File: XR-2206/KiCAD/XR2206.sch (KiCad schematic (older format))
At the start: 15 parts, among them J1 CONN_3, J2 CONN_2, U1 XR2206

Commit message: updating theremin related files
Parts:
- removed C3: 1UF, symbol CAPAPOL
- added C3: 1uF, symbol CP1
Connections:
- wire segments 41 -> 52
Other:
- note added: "S\nV\nG"
- note removed: "G\nV\nS"
- moved on the sheet: C1, C2, J1, J2, MTG1, MTG2, R1, R2, R3, R4, R5, R6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

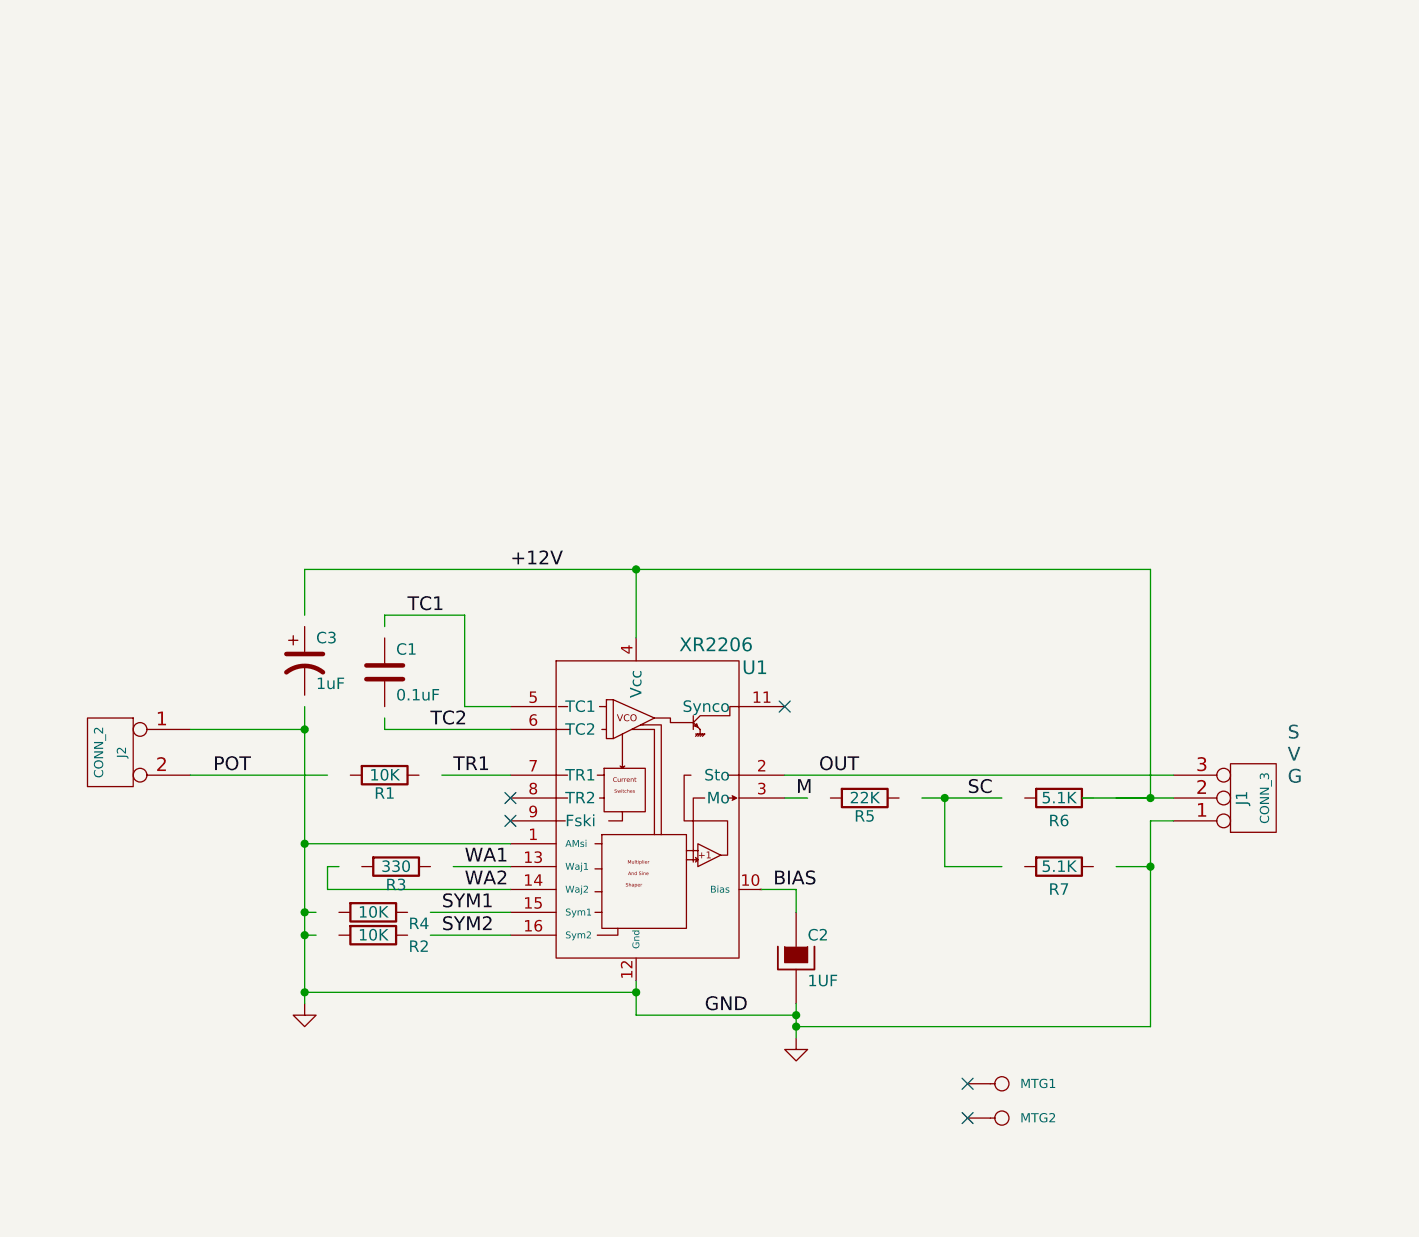
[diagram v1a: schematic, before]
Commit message: Worked on X3 version of XR-2206 and X3 version of BrBdPwrSply
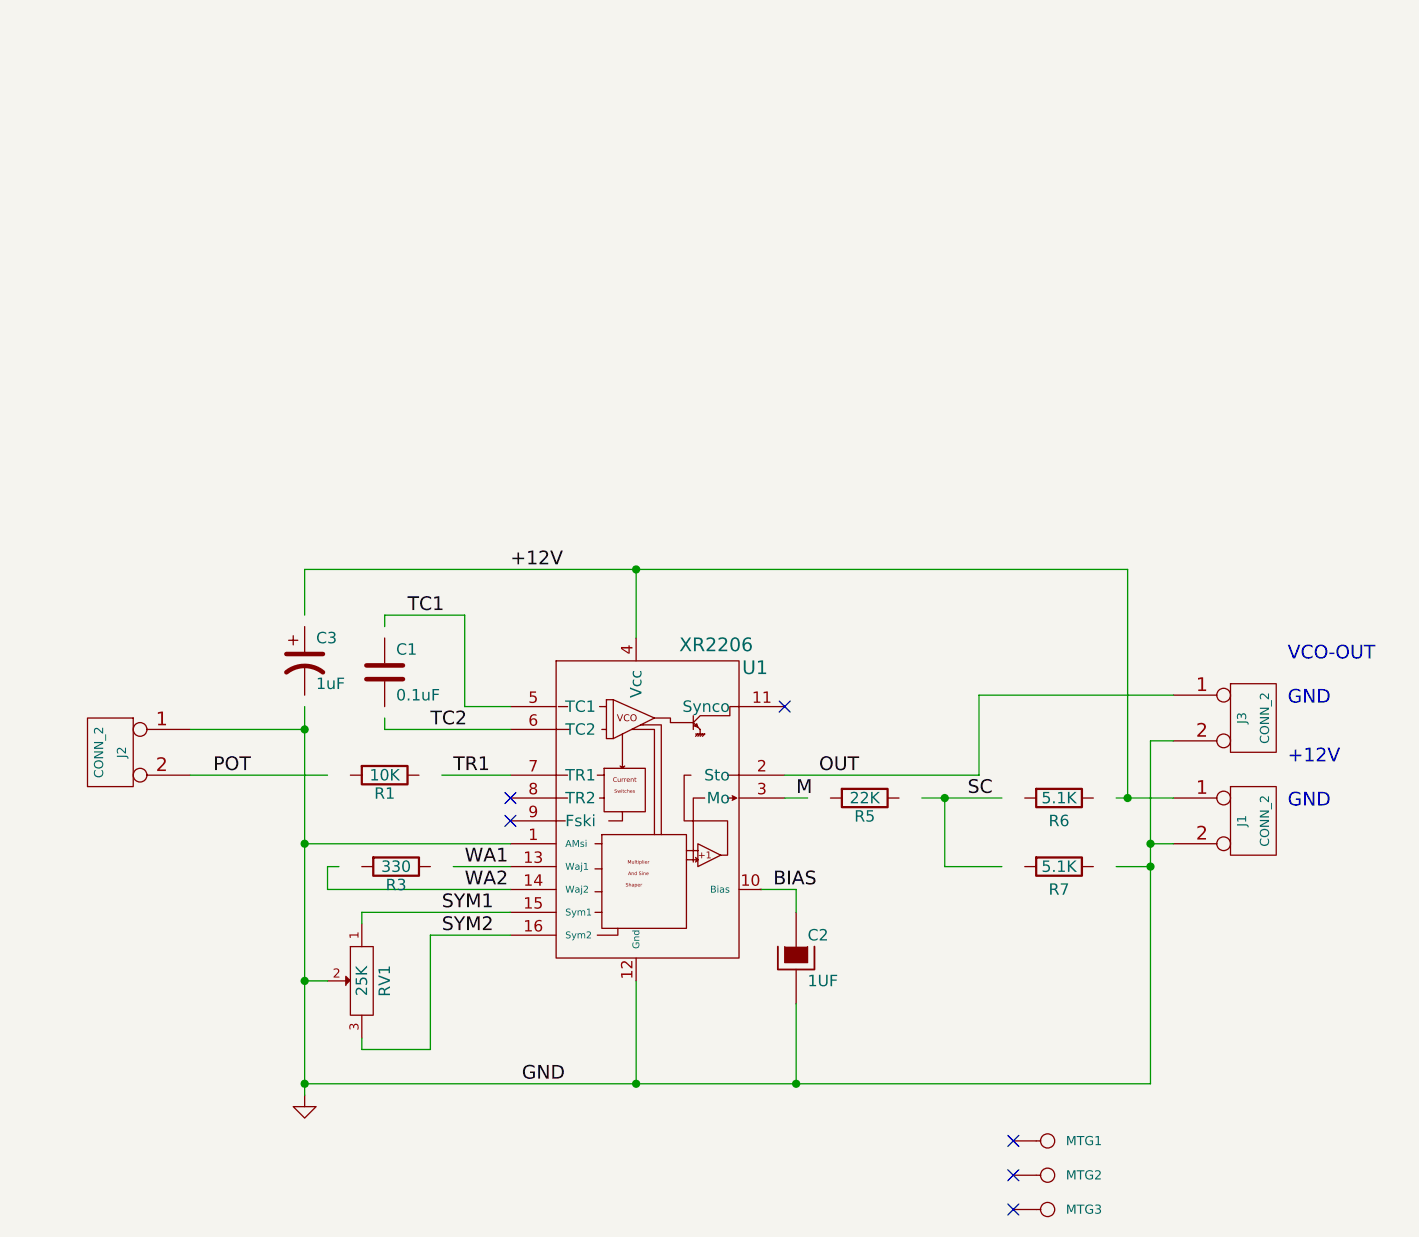
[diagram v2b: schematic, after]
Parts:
- removed J1: CONN_3, symbol CONN_3
- removed R2, R4: 10K, symbol R
- added J1, J3: CONN_2, symbol CONN_2
- added MTG3: CONN_1, symbol CONN_1
- added RV1: 25K, symbol POT
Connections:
- wire segments 52 -> 43
- no-connect marks 5 -> 6
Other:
- note added: "+12V\n\nGND"
- note added: "VCO-OUT\n\nGND"
- note removed: "S\nV\nG"
- moved on the sheet: MTG1, MTG2
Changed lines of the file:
@@
-EESchema Schematic File Version 2  date 13/02/2013 09:23:48
+EESchema Schematic File Version 2  date 15/02/2013 13:58:34
 LIBS:power
 LIBS:device
@@
 Sheet 1 1
 Title "XR-2206"
-Date "13 feb 2013"
+Date "15 feb 2013"
 Rev "X2"
 Comp ""
@@
 Comment4 ""
 $EndDescr
+NoConn ~ 6950 5750
+$Comp
+L CONN_1 MTG3
+U 1 1 511E84D9
+P 7100 5750
+F 0 "MTG3" H 7180 5750 40  0000 L CNN
+F 1 "CONN_1" H 7100 5805 30  0001 C CNN
+	1    7100 5750
+	1    0    0    -1
+$EndComp
+Wire Wire Line
+	7400 3950 7650 3950
+Wire Wire Line
+	7650 3500 6800 3500
+Wire Wire Line
+	6800 3500 6800 3850
+Wire Wire Line
+	6800 3850 5950 3850
+Wire Wire Line
+	4400 5050 4400 4550
+Wire Wire Line
+	4400 5050 4100 5050
+Wire Wire Line
+	4100 5050 4100 5000
+Wire Wire Line
+	4100 4500 4100 4450
+Wire Wire Line
+	4100 4450 4750 4450
+Connection ~ 6650 3950
+Wire Wire Line
+	6550 3950 6900 3950
+Connection ~ 3850 3650
+Wire Wire Line
+	3350 3650 3850 3650
+Connection ~ 5300 5200
+Wire Wire Line
+	5300 4750 5300 5200
+Wire Wire Line
+	7450 2950 3850 2950
+Wire Wire Line
+	7450 2950 7450 3950
+Wire Wire Line
+	4400 4550 4750 4550
+Wire Wire Line
+	4750 4250 4500 4250
+Connection ~ 3850 5200
+Wire Wire Line
+	5300 3250 5300 2950
+Wire Wire Line
+	3850 2950 3850 3150
+Wire Wire Line
+	6000 5200 6000 4850
+Wire Wire Line
+	4200 3200 4200 3150
+Wire Wire Line
+	4200 3150 4550 3150
+Wire Wire Line
+	4550 3150 4550 3550
+Wire Wire Line
+	4550 3550 4750 3550
+Wire Wire Line
+	4450 3850 4750 3850
+Wire Wire Line
+	4750 3650 4200 3650
+Wire Wire Line
+	4200 3650 4200 3600
+Wire Wire Line
+	5850 4350 6000 4350
+Wire Wire Line
+	6000 4350 6000 4450
+Wire Wire Line
+	3850 4150 4750 4150
+Connection ~ 3850 4150
+Connection ~ 5300 2950
+Wire Wire Line
+	3850 5250 3850 3550
+Wire Wire Line
+	4750 4350 3950 4350
+Wire Wire Line
+	3950 4350 3950 4250
+Wire Wire Line
+	3950 4250 4000 4250
+Wire Wire Line
+	3850 5200 7550 5200
+Connection ~ 6000 5200
+Wire Wire Line
+	7550 4150 7650 4150
+Wire Wire Line
+	3950 3850 3350 3850
+Connection ~ 7450 3950
+Wire Wire Line
+	6900 4250 6650 4250
+Wire Wire Line
+	6650 4250 6650 3950
+Wire Wire Line
+	5950 3950 6050 3950
+Wire Wire Line
+	7400 4250 7550 4250
 Connection ~ 7550 4250
 Wire Wire Line
-	7400 4250 7550 4250
-Wire Wire Line
-	5950 3950 6050 3950
-Wire Wire Line
-	6650 3950 6650 4250
-Wire Wire Line
-	6650 4250 6900 4250
-Connection ~ 7550 3950
-Wire Wire Line
-	7400 3950 7550 3950
-Wire Wire Line
-	3950 3850 3350 3850
-Wire Wire Line
-	7650 4050 7550 4050
-Connection ~ 6000 4950
-Wire Wire Line
-	6000 4950 7550 4950
-Wire Wire Line
-	5950 3850 7650 3850
-Connection ~ 3850 4450
-Wire Wire Line
-	3850 4450 3900 4450
-Wire Wire Line
-	4000 4250 3950 4250
-Wire Wire Line
-	3950 4250 3950 4350
-Wire Wire Line
-	3950 4350 4750 4350
-Wire Wire Line
-	3850 4850 3850 4800
-Wire Wire Line
-	3850 4800 3850 4550
-Wire Wire Line
-	3850 4550 3850 4450
-Wire Wire Line
-	3850 4450 3850 4150
-Wire Wire Line
-	3850 4150 3850 3650
-Wire Wire Line
-	3850 3650 3850 3550
-Connection ~ 5300 2950
-Connection ~ 3850 4150
-Wire Wire Line
-	3850 4150 4750 4150
-Wire Wire Line
-	6000 4450 6000 4350
-Wire Wire Line
-	6000 4350 5850 4350
-Wire Wire Line
-	4200 3600 4200 3650
-Wire Wire Line
-	4200 3650 4750 3650
-Wire Wire Line
-	4450 3850 4750 3850
-Wire Wire Line
-	4750 3550 4550 3550
-Wire Wire Line
-	4550 3550 4550 3150
-Wire Wire Line
-	4550 3150 4200 3150
-Wire Wire Line
-	4200 3150 4200 3200
-Wire Wire Line
-	6000 4850 6000 4900
-Wire Wire Line
-	6000 4900 6000 4950
-Wire Wire Line
-	6000 4950 6000 5000
-Wire Wire Line
-	3850 3150 3850 2950
-Wire Wire Line
-	5300 3250 5300 2950
-Wire Wire Line
-	5300 4800 3850 4800
-Connection ~ 3850 4800
-Wire Wire Line
-	4750 4250 4500 4250
-Wire Wire Line
-	4750 4450 4400 4450
-Wire Wire Line
-	3850 4550 3900 4550
-Connection ~ 3850 4550
-Wire Wire Line
-	4400 4550 4750 4550
-Wire Wire Line
-	7550 3950 7550 2950
-Wire Wire Line
-	7250 3950 7550 3950
-Wire Wire Line
-	7550 3950 7650 3950
-Wire Wire Line
-	7550 2950 5300 2950
-Wire Wire Line
-	5300 2950 3850 2950
-Wire Wire Line
-	6000 4900 5300 4900
-Wire Wire Line
-	5300 4900 5300 4800
-Wire Wire Line
-	5300 4800 5300 4750
-Connection ~ 5300 4800
-Connection ~ 6000 4900
-Wire Wire Line
-	3850 3650 3350 3650
-Connection ~ 3850 3650
-Wire Wire Line
-	6550 3950 6650 3950
-Wire Wire Line
-	6650 3950 6900 3950
-Connection ~ 6650 3950
-Wire Wire Line
-	7550 4950 7550 4250
-Wire Wire Line
-	7550 4250 7550 4050
+	3850 4750 3950 4750
+Connection ~ 3850 4750
+Wire Wire Line
+	7550 5200 7550 3700
+Wire Wire Line
+	7550 3700 7650 3700
+Connection ~ 7550 4150
+Text Notes 8150 3550 0    60   ~ 0
+VCO-OUT\n\nGND
+$Comp
+L CONN_2 J3
+U 1 1 511E7A29
+P 8000 3600
+F 0 "J3" V 7950 3600 40  0000 C CNN
+F 1 "CONN_2" V 8050 3600 40  0000 C CNN
+	1    8000 3600
+	1    0    0    -1
+$EndComp
+$Comp
+L CONN_2 J1
+U 1 1 511E7A25
+P 8000 4050
+F 0 "J1" V 7950 4050 40  0000 C CNN
+F 1 "CONN_2" V 8050 4050 40  0000 C CNN
+	1    8000 4050
+	1    0    0    -1
+$EndComp
+$Comp
+L POT RV1
+U 1 1 511E791A
+P 4100 4750
+F 0 "RV1" H 4100 4650 50  0000 C CNN
+F 1 "25K" H 4100 4750 50  0000 C CNN
+	1    4100 4750
+	0    -1   1    0
+$EndComp
 $Comp
 L CP1 C3
@@
 L CONN_1 MTG2
 U 1 1 501125B1
-P 6900 5350
-F 0 "MTG2" H 6980 5350 40  0000 L CNN
-F 1 "CONN_1" H 6900 5405 30  0001 C CNN
-	1    6900 5350
-	1    0    0    -1
-$EndComp
-NoConn ~ 6750 5350
+P 7100 5600
+F 0 "MTG2" H 7180 5600 40  0000 L CNN
+F 1 "CONN_1" H 7100 5655 30  0001 C CNN
+	1    7100 5600
+	1    0    0    -1
+$EndComp
+NoConn ~ 6950 5600
 $Comp
 L R R5
@@
 	-1   0    0    -1
 $EndComp
-Text Notes 8150 3900 0    60   ~ 0
-S\nV\nG
-NoConn ~ 6750 5200
+Text Notes 8150 4000 0    60   ~ 0
++12V\n\nGND
+NoConn ~ 6950 5450
 $Comp
 L CONN_1 MTG1
 U 1 1 4FDBED61
-P 6900 5200
-F 0 "MTG1" H 6980 5200 40  0000 L CNN
-F 1 "CONN_1" H 6900 5255 30  0001 C CNN
-	1    6900 5200
-	1    0    0    -1
-$EndComp
-Text Label 5600 4900 0    60   ~ 0
+P 7100 5450
+F 0 "MTG1" H 7180 5450 40  0000 L CNN
+F 1 "CONN_1" H 7100 5505 30  0001 C CNN
+	1    7100 5450
+	1    0    0    -1
+$EndComp
+Text Label 4800 5200 0    60   ~ 0
 GND
 Text Label 4750 2950 0    60   ~ 0
@@
 NoConn ~ 4750 4050
 NoConn ~ 4750 3950
-$Comp
-L CONN_3 J1
-U 1 1 4FDBE66A
-P 8000 3950
-F 0 "J1" V 7950 3950 50  0000 C CNN
-F 1 "CONN_3" V 8050 3950 40  0000 C CNN
-	1    8000 3950
-	1    0    0    1
-$EndComp
-$Comp
-L R R2
-U 1 1 4FDBE59E
-P 4150 4550
-F 0 "R2" V 4200 4750 50  0000 C CNN
-F 1 "10K" V 4150 4550 50  0000 C CNN
-	1    4150 4550
-	0    1    1    0
-$EndComp
-$Comp
-L R R4
-U 1 1 4FDBE58B
-P 4150 4450
-F 0 "R4" V 4200 4650 50  0000 C CNN
-F 1 "10K" V 4150 4450 50  0000 C CNN
-	1    4150 4450
-	0    1    1    0
-$EndComp
 $Comp
 L R R3
@@
 $EndComp
 $Comp
-L GND #PWR01
-U 1 1 4FDBC7B9
-P 6000 5000
-F 0 "#PWR01" H 6000 5000 30  0001 C CNN
-F 1 "GND" H 6000 4930 30  0001 C CNN
-	1    6000 5000
-	1    0    0    -1
-$EndComp
-$Comp
 L CAPAPOL C2
 U 1 1 4FDBC7A6
@@
 $EndComp
 $Comp
-L GND #PWR02
+L GND #PWR01
 U 1 1 4FDBC71A
-P 3850 4850
-F 0 "#PWR02" H 3850 4850 30  0001 C CNN
-F 1 "GND" H 3850 4780 30  0001 C CNN
-	1    3850 4850
-	1    0    0    -1
-$EndComp
+P 3850 5250
+F 0 "#PWR01" H 3850 5250 30  0001 C CNN
+F 1 "GND" H 3850 5180 30  0001 C CNN
+	1    3850 5250
+	1    0    0    -1
+$EndComp

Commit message: Integr theremin
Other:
- note added: "G\n\nADJ"
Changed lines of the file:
@@
-EESchema Schematic File Version 2  date 15/02/2013 13:58:34
+EESchema Schematic File Version 2  date Fri 15 Feb 2013 06:24:37 PM EST
 LIBS:power
 LIBS:device
@@
 LIBS:atmel
 LIBS:contrib
-LIBS:EXAR
 LIBS:XR2206-cache
 EELAYER 25  0
@@
 Comment4 ""
 $EndDescr
+Text Notes 2850 3700 2    60   ~ 0
+G\n\nADJ
 NoConn ~ 6950 5750
 $Comp

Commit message: Updated libraries and XR-2206 board schematic
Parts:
- C3: value 1uF -> 4.7uF
- R3: value 330 -> 220
- R5: value 22K -> 10K
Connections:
- wire segments 43 -> 42
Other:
- moved on the sheet: J1, J3
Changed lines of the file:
@@
-EESchema Schematic File Version 2  date Fri 15 Feb 2013 06:24:37 PM EST
+EESchema Schematic File Version 2  date 06/03/2013 12:50:37
 LIBS:power
 LIBS:device
@@
 LIBS:contrib
 LIBS:XR2206-cache
-EELAYER 25  0
+EELAYER 27 0
 EELAYER END
 $Descr A 11000 8500
@@
 Sheet 1 1
 Title "XR-2206"
-Date "15 feb 2013"
-Rev "X2"
+Date "6 mar 2013"
+Rev "X3"
 Comp ""
 Comment1 ""
@@
 F 0 "MTG3" H 7180 5750 40  0000 L CNN
 F 1 "CONN_1" H 7100 5805 30  0001 C CNN
+F 2 "" H 7100 5750 60  0001 C CNN
+F 3 "" H 7100 5750 60  0001 C CNN
 	1    7100 5750
 	1    0    0    -1
 $EndComp
 Wire Wire Line
-	7400 3950 7650 3950
-Wire Wire Line
-	7650 3500 6800 3500
-Wire Wire Line
-	6800 3500 6800 3850
+	3850 2950 7700 2950
+Wire Wire Line
+	7650 3850 6800 3850
 Wire Wire Line
 	6800 3850 5950 3850
@@
 Wire Wire Line
 	5300 4750 5300 5200
-Wire Wire Line
-	7450 2950 3850 2950
 Wire Wire Line
 	7450 2950 7450 3950
@@
 	3950 4250 4000 4250
 Wire Wire Line
-	3850 5200 7550 5200
+	7550 5200 3850 5200
 Connection ~ 6000 5200
 Wire Wire Line
-	7550 4150 7650 4150
+	7550 3150 7700 3150
 Wire Wire Line
 	3950 3850 3350 3850
-Connection ~ 7450 3950
 Wire Wire Line
 	6900 4250 6650 4250
@@
 Connection ~ 3850 4750
 Wire Wire Line
-	7550 5200 7550 3700
-Wire Wire Line
-	7550 3700 7650 3700
-Connection ~ 7550 4150
-Text Notes 8150 3550 0    60   ~ 0
+	7550 3150 7550 5200
+Wire Wire Line
+	7550 4050 7650 4050
+Text Notes 8150 3900 0    60   ~ 0
 VCO-OUT\n\nGND
 $Comp
 L CONN_2 J3
 U 1 1 511E7A29
-P 8000 3600
-F 0 "J3" V 7950 3600 40  0000 C CNN
-F 1 "CONN_2" V 8050 3600 40  0000 C CNN
-	1    8000 3600
+P 8000 3950
+F 0 "J3" V 7950 3950 40  0000 C CNN
+F 1 "CONN_2" V 8050 3950 40  0000 C CNN
+F 2 "" H 8000 3950 60  0001 C CNN
+F 3 "" H 8000 3950 60  0001 C CNN
+	1    8000 3950
 	1    0    0    -1
 $EndComp
@@
 L CONN_2 J1
 U 1 1 511E7A25
-P 8000 4050
-F 0 "J1" V 7950 4050 40  0000 C CNN
-F 1 "CONN_2" V 8050 4050 40  0000 C CNN
-	1    8000 4050
+P 8050 3050
+F 0 "J1" V 8000 3050 40  0000 C CNN
+F 1 "CONN_2" V 8100 3050 40  0000 C CNN
+F 2 "" H 8050 3050 60  0001 C CNN
+F 3 "" H 8050 3050 60  0001 C CNN
+	1    8050 3050
 	1    0    0    -1
 $EndComp
@@
 F 0 "RV1" H 4100 4650 50  0000 C CNN
 F 1 "25K" H 4100 4750 50  0000 C CNN
+F 2 "" H 4100 4750 60  0001 C CNN
+F 3 "" H 4100 4750 60  0001 C CNN
 	1    4100 4750
 	0    -1   1    0
@@
 P 3850 3350
 F 0 "C3" H 3900 3450 50  0000 L CNN
-F 1 "1uF" H 3900 3250 50  0000 L CNN
+F 1 "4.7uF" H 3900 3250 50  0000 L CNN
+F 2 "" H 3850 3350 60  0001 C CNN
+F 3 "" H 3850 3350 60  0001 C CNN
 	1    3850 3350
 	1    0    0    -1
@@
 F 0 "MTG2" H 7180 5600 40  0000 L CNN
 F 1 "CONN_1" H 7100 5655 30  0001 C CNN
+F 2 "" H 7100 5600 60  0001 C CNN
+F 3 "" H 7100 5600 60  0001 C CNN
 	1    7100 5600
 	1    0    0    -1
@@
 P 6300 3950
 F 0 "R5" V 6380 3950 50  0000 C CNN
-F 1 "22K" V 6300 3950 50  0000 C CNN
+F 1 "10K" V 6300 3950 50  0000 C CNN
+F 2 "" H 6300 3950 60  0001 C CNN
+F 3 "" H 6300 3950 60  0001 C CNN
 	1    6300 3950
 	0    1    1    0
@@
 F 0 "R7" V 7250 4250 50  0000 C CNN
 F 1 "5.1K" V 7150 4250 50  0000 C CNN
+F 2 "" H 7150 4250 60  0001 C CNN
+F 3 "" H 7150 4250 60  0001 C CNN
 	1    7150 4250
 	0    1    1    0
@@
 F 0 "R6" V 7250 3950 50  0000 C CNN
 F 1 "5.1K" V 7150 3950 50  0000 C CNN
+F 2 "" H 7150 3950 60  0001 C CNN
+F 3 "" H 7150 3950 60  0001 C CNN
 	1    7150 3950
 	0    1    1    0
@@
 F 0 "J2" V 2950 3750 40  0000 C CNN
 F 1 "CONN_2" V 3050 3750 40  0000 C CNN
+F 2 "" H 3000 3750 60  0001 C CNN
+F 3 "" H 3000 3750 60  0001 C CNN
 	1    3000 3750
 	-1   0    0    -1
 $EndComp
-Text Notes 8150 4000 0    60   ~ 0
+Text Notes 8200 3000 0    60   ~ 0
 +12V\n\nGND
 NoConn ~ 6950 5450
@@
 F 0 "MTG1" H 7180 5450 40  0000 L CNN
 F 1 "CONN_1" H 7100 5505 30  0001 C CNN
+F 2 "" H 7100 5450 60  0001 C CNN
+F 3 "" H 7100 5450 60  0001 C CNN
 	1    7100 5450
 	1    0    0    -1
@@
 P 4250 4250
 F 0 "R3" V 4330 4250 50  0000 C CNN
-F 1 "330" V 4250 4250 50  0000 C CNN
+F 1 "220" V 4250 4250 50  0000 C CNN
+F 2 "" H 4250 4250 60  0001 C CNN
+F 3 "" H 4250 4250 60  0001 C CNN
 	1    4250 4250
 	0    1    1    0
@@
 F 0 "C2" H 6050 4750 50  0000 L CNN
 F 1 "1UF" H 6050 4550 50  0000 L CNN
+F 2 "" H 6000 4650 60  0001 C CNN
+F 3 "" H 6000 4650 60  0001 C CNN
 	1    6000 4650
 	1    0    0    -1
@@
 F 0 "C1" H 4250 3500 50  0000 L CNN
 F 1 "0.1uF" H 4250 3300 50  0000 L CNN
+F 2 "" H 4200 3400 60  0001 C CNN
+F 3 "" H 4200 3400 60  0001 C CNN
 	1    4200 3400
 	1    0    0    -1
@@
 F 0 "#PWR01" H 3850 5250 30  0001 C CNN
 F 1 "GND" H 3850 5180 30  0001 C CNN
+F 2 "" H 3850 5250 60  0001 C CNN
+F 3 "" H 3850 5250 60  0001 C CNN
 	1    3850 5250
 	1    0    0    -1
@@
 F 0 "R1" V 4280 3850 50  0000 C CNN
 F 1 "10K" V 4200 3850 50  0000 C CNN
+F 2 "" H 4200 3850 60  0001 C CNN
+F 3 "" H 4200 3850 60  0001 C CNN
 	1    4200 3850
 	0    1    1    0
@@
 F 0 "U1" H 5820 4720 60  0000 C CNN
 F 1 "XR2206" H 5650 4820 60  0000 C CNN
+F 2 "" H 5300 4050 60  0001 C CNN
+F 3 "" H 5300 4050 60  0001 C CNN
 	1    5300 4050
 	1    0    0    -1
 $EndComp
+Wire Wire Line
+	7450 3950 7400 3950
+Connection ~ 7450 2950
 $EndSCHEMATC
